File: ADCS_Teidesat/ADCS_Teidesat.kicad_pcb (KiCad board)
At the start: 2 copper layers, 90.2 x 95.9 mm, 26 parts, among them IC2 L86-M33, IC3 MAX2659ELT+T, IC5 TMS5703137DPGEQQ1, IC7 LSM6DSV16XTR, IC8 LIS2MDLTR, Y1 ATX-H13-F-16.000MHz-G100-T

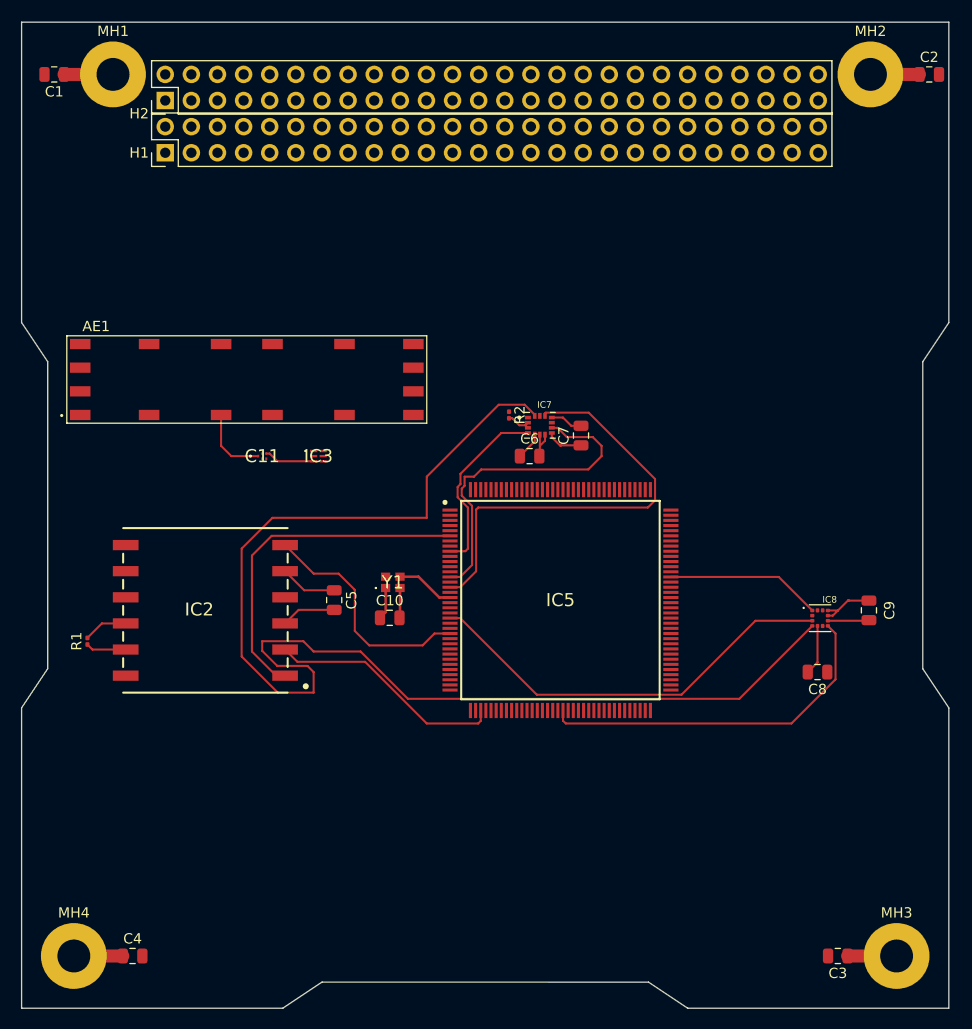
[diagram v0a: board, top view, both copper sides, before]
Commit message: Nuevo enrutado y correcciones de nombres y plantilla.
Co-Authored-By: Angel-Castro-Vega <236372966+Angel-Castro-Vega@users.noreply.github.com>
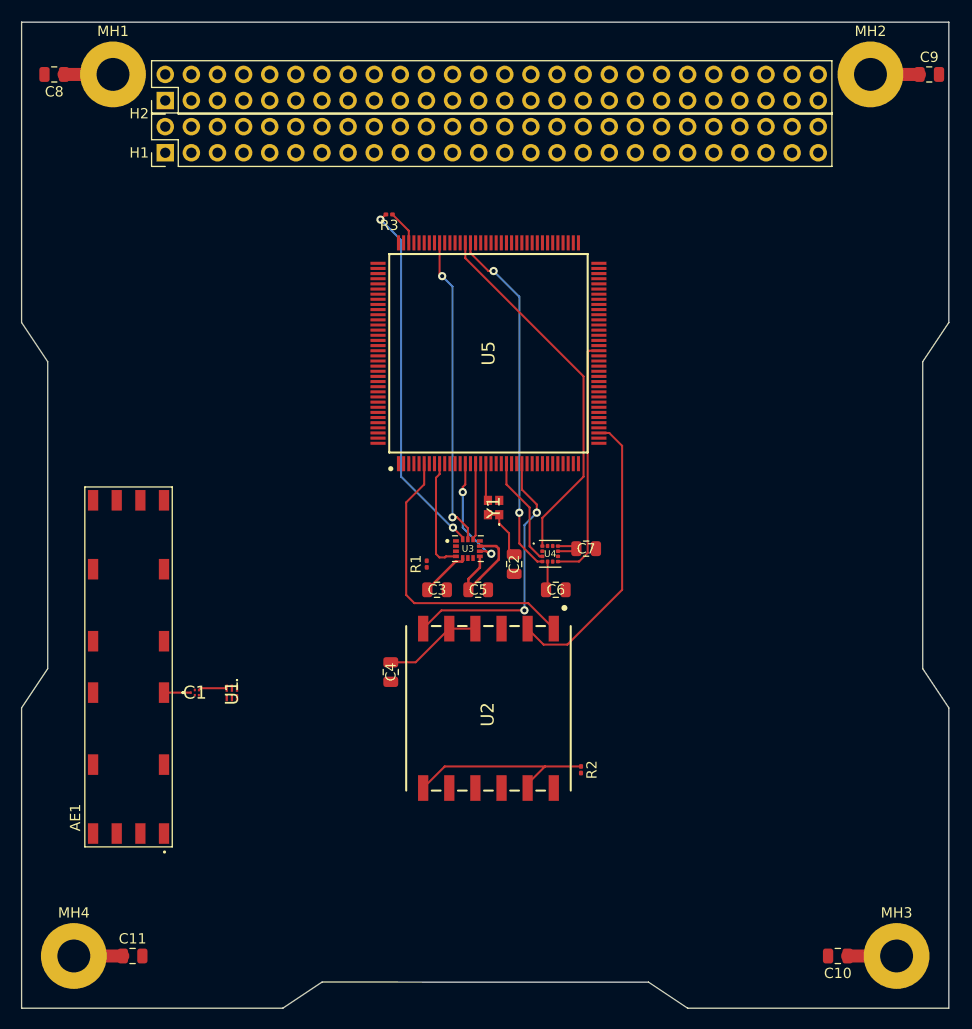
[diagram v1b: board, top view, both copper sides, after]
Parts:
- removed the C10 at (137.4, 108.7)
- removed the C11 at (125.0, 93.0)
- removed the C8 at (179.0, 114.0)
- removed the C9 at (184.0, 108.0)
- removed IC2: L86-M33, Huellas ADCS:L80-M39
- removed IC3: MAX2659ELT+T, Huellas ADCS:MAX2659ELTT
- removed IC5: TMS5703137DPGEQQ1, Huellas ADCS:QFP50P2200X2200X160-144N
- removed IC7: LSM6DSV16XTR, Huellas ADCS:XDCR_LSM6DSV16XTR
- removed IC8: LIS2MDLTR, Huellas ADCS:PQFN50P200X200X70-12N
- added C1: F6QA1G581M2QZ-J, Huellas ADCS:F6QA1G581M2QZJ, F.Cu at (118.4, 116.0)
- added C2: 100n, Capacitor_SMD:C_0805_2012Metric, F.Cu at (149.5, 103.5)
- added C3: 100n, Capacitor_SMD:C_0805_2012Metric, F.Cu at (142.0, 106.0)
- added C4: 100n, Capacitor_SMD:C_0805_2012Metric, F.Cu at (137.5, 114.0)
- added R3: 33, Resistor_SMD:R_0201_0603Metric, F.Cu at (137.3, 69.5)
- added U1: MAX2659ELT+T, Huellas ADCS:MAX2659ELTT, F.Cu at (122.0, 116.0)
- added U2: L86-M33, Huellas ADCS:L80-M39, F.Cu at (141.9, 125.3)
- added U3: LSM6DSV16XTR, Huellas ADCS:XDCR_LSM6DSV16XTR, F.Cu at (145.0, 102.0)
- added U4: LIS2MDLTR, Huellas ADCS:PQFN50P200X200X70-12N, F.Cu at (153.0, 102.5)
- added U5: TMS5703137DPGEQQ1, Huellas ADCS:QFP50P2200X2200X160-144N, F.Cu at (147.0, 83.0)
- C6: value 100n -> 220n
- moved R2 35.2 mm to (156.0, 123.5)
- moved R1 33.8 mm to (141.0, 103.5)
- moved AE1 30.2 mm to (112.0, 113.5), turned to 90 degrees
- moved C5 14.0 mm to (146.0, 106.0), turned to 0 degrees
- moved C6 13.2 mm to (153.6, 106.0), turned to 180 degrees
- moved Y1 12.2 mm to (147.5, 98.0), turned to 90 degrees
- moved C7 11.0 mm to (156.5, 102.0), turned to 0 degrees
- renumbered C3 to C10, C4 to C11, C1 to C8, C2 to C9
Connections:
- C6 pad 1: +3V3 -> GND
- C6 pad 2: GND -> Net-(U4-C1)
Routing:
- net /IMU/MAGNETÓMETRO: track 123.6 -> 0.00 mm
- net /CS_IMU: track 42.7 -> 7.45 mm
- net /SIMO_IMU: track 0.00 -> 35.2 mm, vias 0 -> 2
- net /MAGNETÓMETRO: track 0.00 -> 34.5 mm, vias 0 -> 2
- net /CS_MAGNETÓMETRO: track 41.3 -> 10.6 mm
- net /CLOCK_IMU: track 0.00 -> 30.2 mm, vias 0 -> 2
- net +3V3: track 24.5 -> 53.7 mm
- net GND: track 26.1 -> 0.00 mm
- net /INT2: track 32.5 -> 11.4 mm, vias 0 -> 2
- net /SPC_MAG.: track 15.1 -> 35.9 mm
- net /INT_MAGNETÓMETRO: track 34.9 -> 23.9 mm
- net /INT1: track 17.9 -> 11.0 mm
- net /DATA_OUT: track 23.1 -> 28.8 mm
- net Net-(IC8-C1): track 4.87 -> 0.00 mm
- net /ANTENNA: track 7.02 -> 2.56 mm
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
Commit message: Plano GND y Plano 3V3
He modificado la PCB de dos capas a cuatro capas. Con esto, hemos conseguido una capa  extra de GND y he añadido el plano de potencia.
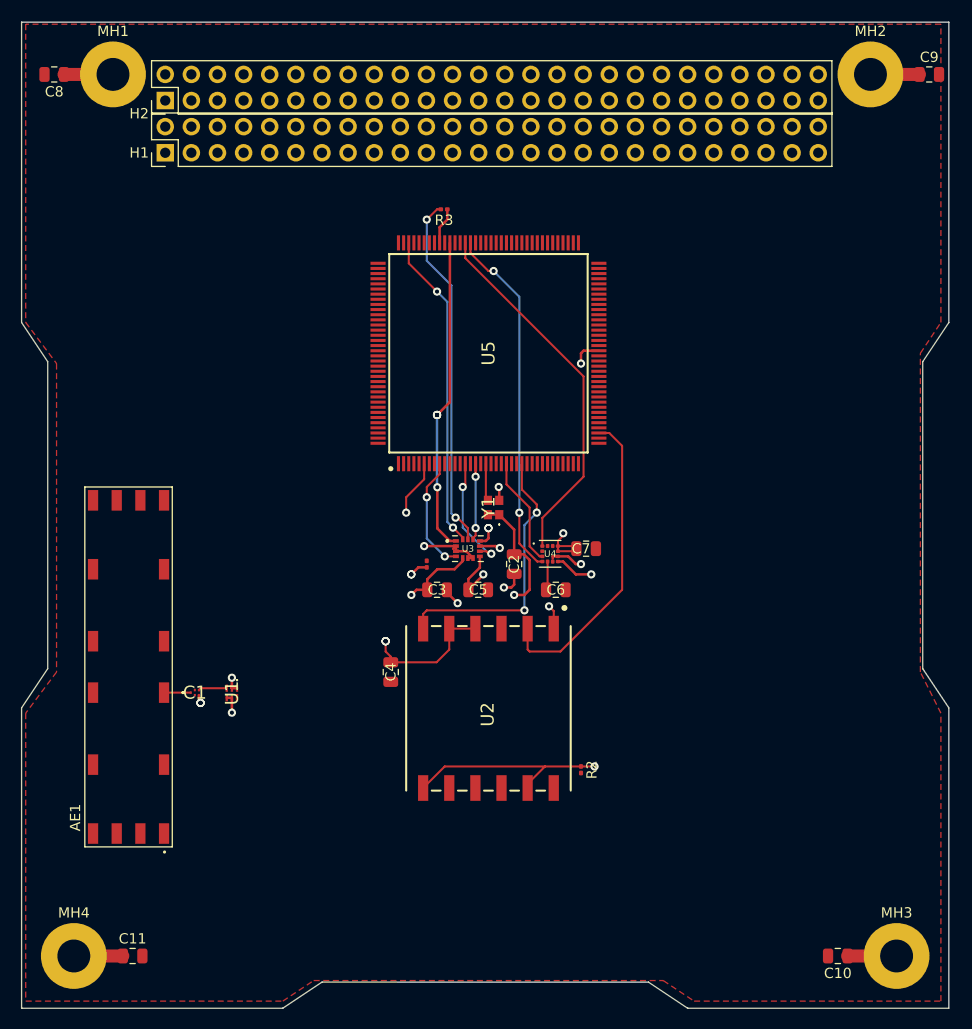
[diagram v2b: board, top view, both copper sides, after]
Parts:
- moved R3 5.36 mm to (142.7, 69.0)
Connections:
- R3 pad 1: Net-(U5-N2HET1[08]) -> Net-(U5-MIBSPI5CLK)
- R3 pad 2: /SIMO_IMU -> /CLOCK_IMU
- U3 pad 1: GND -> /SOMI_IMU
- U5 pad 100: /CLOCK_IMU -> Net-(U5-MIBSPI5CLK)
- U5 pad 106: Net-(U5-N2HET1[08]) -> /SIMO_IMU
- U5 pad 98: unconnected-(U5-MIBSPI5SOMI[0]-Pad98) -> /SOMI_IMU
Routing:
- net /SOMI_IMU: track 0.00 -> 30.6 mm, vias 0 -> 4
- net +3V3: track 53.7 -> 82.3 mm, vias 0 -> 12
- net GND: track 0.00 -> 24.8 mm, vias 0 -> 11
- net /CLOCK_IMU: track 30.2 -> 34.4 mm
- net /SIMO_IMU: track 35.2 -> 31.1 mm
- net /INT_MAGNETÓMETRO: track 23.9 -> 27.5 mm, vias 0 -> 2
- net Net-(U5-MIBSPI5CLK): track 0.00 -> 3.57 mm
- net Net-(U5-N2HET1[08]): track 3.42 -> 0.00 mm
- net /DATA_OUT: track 28.8 -> 30.6 mm
- net /1PPS: track 25.9 -> 26.8 mm
- net /INT1: track 11.0 -> 11.3 mm, vias 0 -> 2
- net /DATA_IN: track 29.2 -> 29.0 mm, vias 0 -> 2
- net /CS_IMU: vias 0 -> 2
- added copper zone on In1.Cu, net +3V3
- added copper zone on F.Cu, net GND
- added copper zone on In2.Cu, net GND
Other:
- copper layers 2 -> 4

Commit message: Mejora del enrutado y las conexiones de los componentes, además de la  modificación en la distribución de los planos
Optimización de las conexiones, liberando la capa TOP relazándolas en la capa BOTTON. Modificación de la distribución de los planos. Actualmente: TOP Layer (Plano de conexiones 1), Inner Layer 1 (GND), Inner Layer 2 (3V3) y BOTTON Layer (Plano de conexiones 2)
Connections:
- H1 pad 47: unconnected-(H1-Pin_47-Pad47) -> +3V3
- H1 pad 48: unconnected-(H1-Pin_48-Pad48) -> +3V3
- H1 pad 49: unconnected-(H1-Pin_49-Pad49) -> +3V3
- H1 pad 50: unconnected-(H1-Pin_50-Pad50) -> +3V3
- H1 pad 51: unconnected-(H1-Pin_51-Pad51) -> +3V3
- H1 pad 52: unconnected-(H1-Pin_52-Pad52) -> +3V3
- H2 pad 18: unconnected-(H2-Pin_18-Pad18) -> +3V3
- H2 pad 19: unconnected-(H2-Pin_19-Pad19) -> +3V3
- H2 pad 20: unconnected-(H2-Pin_20-Pad20) -> +3V3
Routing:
- net GND: track 24.8 -> 59.1 mm, vias 11 -> 28
- net /DATA_IN: track 29.0 -> 37.1 mm
- net +3V3: track 82.3 -> 76.5 mm, vias 12 -> 15
- net /DATA_OUT: track 30.6 -> 33.4 mm, vias 0 -> 2
- net /INT1: track 11.3 -> 11.8 mm
- added copper zone on B.Cu, net (none)
- added copper zone on F.Cu, net (none)
- added copper zone on In2.Cu, net +3V3
- added copper zone on In1.Cu, net GND
- removed copper zone on In1.Cu, net +3V3
- removed copper zone on F.Cu, net GND
- removed copper zone on In2.Cu, net GND

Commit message: Últimas modificaciones de la V.0.1.
Se han realizado las últimas modificaciones en del diseño de la PCB, se han nombrado las capas, y además, se han añadido las huellas correctas de cada componente.
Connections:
- H2 pad 29: unconnected-(H2-Pin_29-Pad29) -> GND
- H2 pad 30: unconnected-(H2-Pin_30-Pad30) -> GND
- H2 pad 31: unconnected-(H2-Pin_31-Pad31) -> GND
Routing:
- net GND: track 59.1 -> 67.7 mm, vias 28 -> 29
